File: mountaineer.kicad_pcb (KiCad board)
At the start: 2 copper layers, 50 x 79 mm, 69 parts, among them J1 USB_C_Receptacle, J2 CAT, J3 AUDIO, SW1 VCCIO, U1 TUSB2036, U2 FT232RL, U3 HS-100B, U4 TPS76333, U5 SN75240, U6 TPS2041, Y1 AWSCR-6.00CPLA

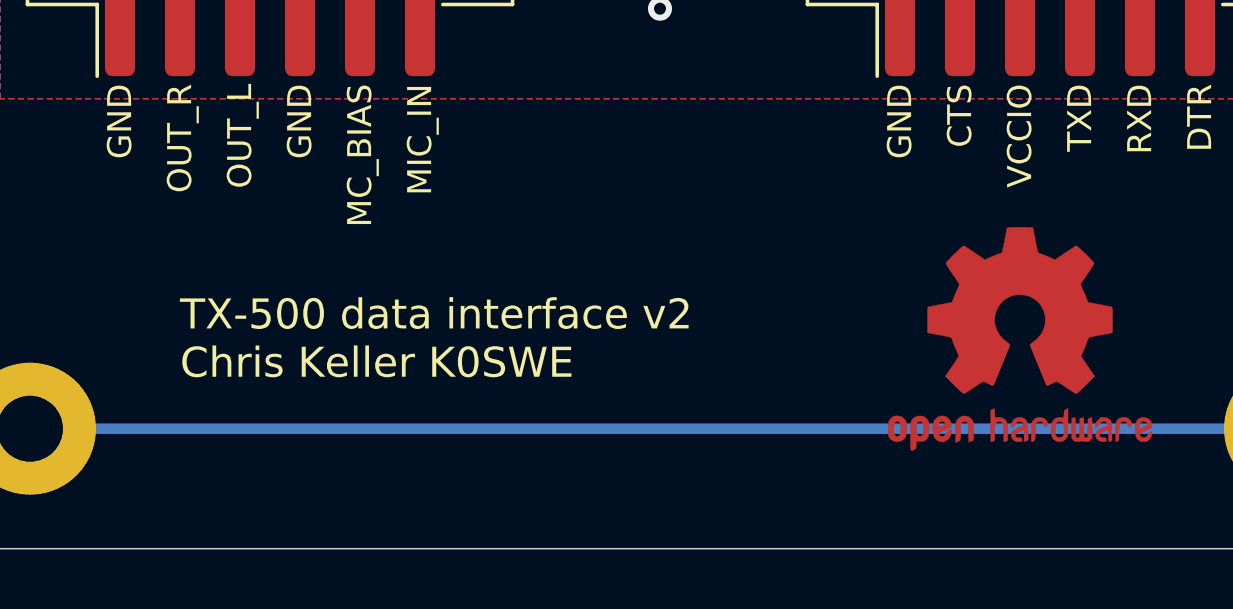
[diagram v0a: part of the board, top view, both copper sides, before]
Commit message: Rename project
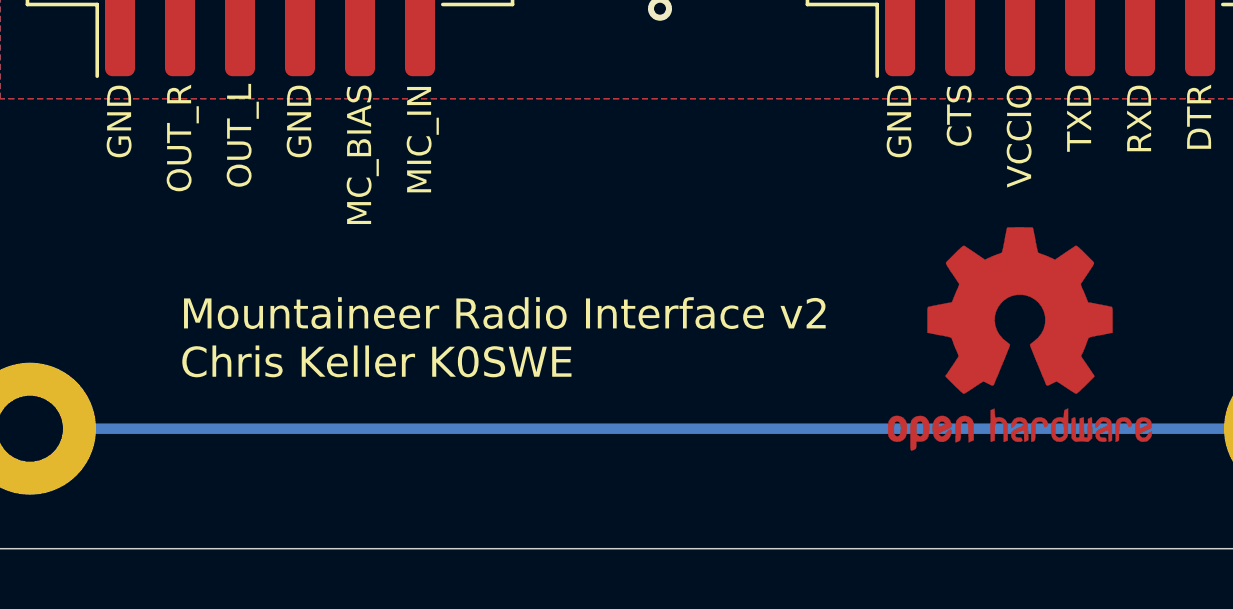
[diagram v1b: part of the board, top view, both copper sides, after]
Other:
- board text added: "Mountaineer Radio Interface v2 Chris Keller K0SWE"
- board text added: "https://github.com/k0swe/mountaineer"
- board text removed: "TX-500 data interface v2 Chris Keller K0SWE"
- board text removed: "https://github.com/k0swe/tx500-data-interface"

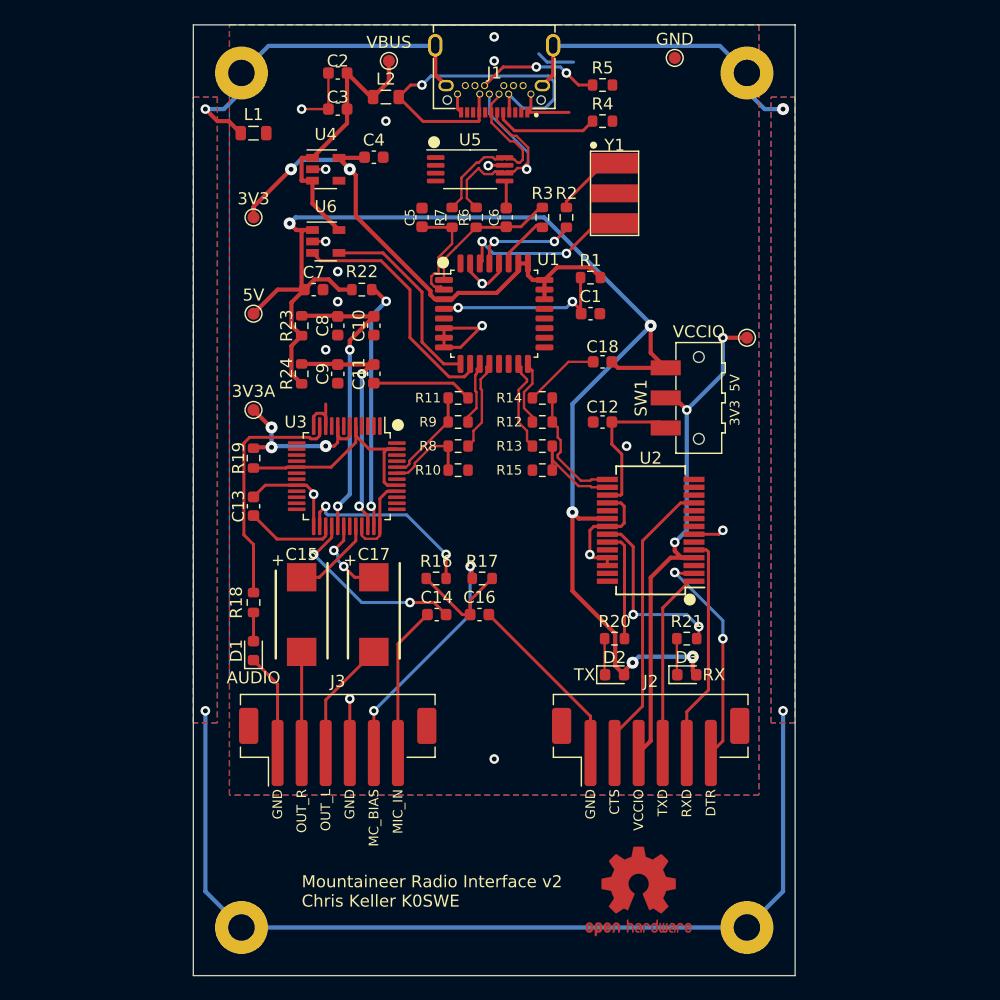
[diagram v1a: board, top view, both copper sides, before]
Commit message: Add pullup resistor to overcurrent protection
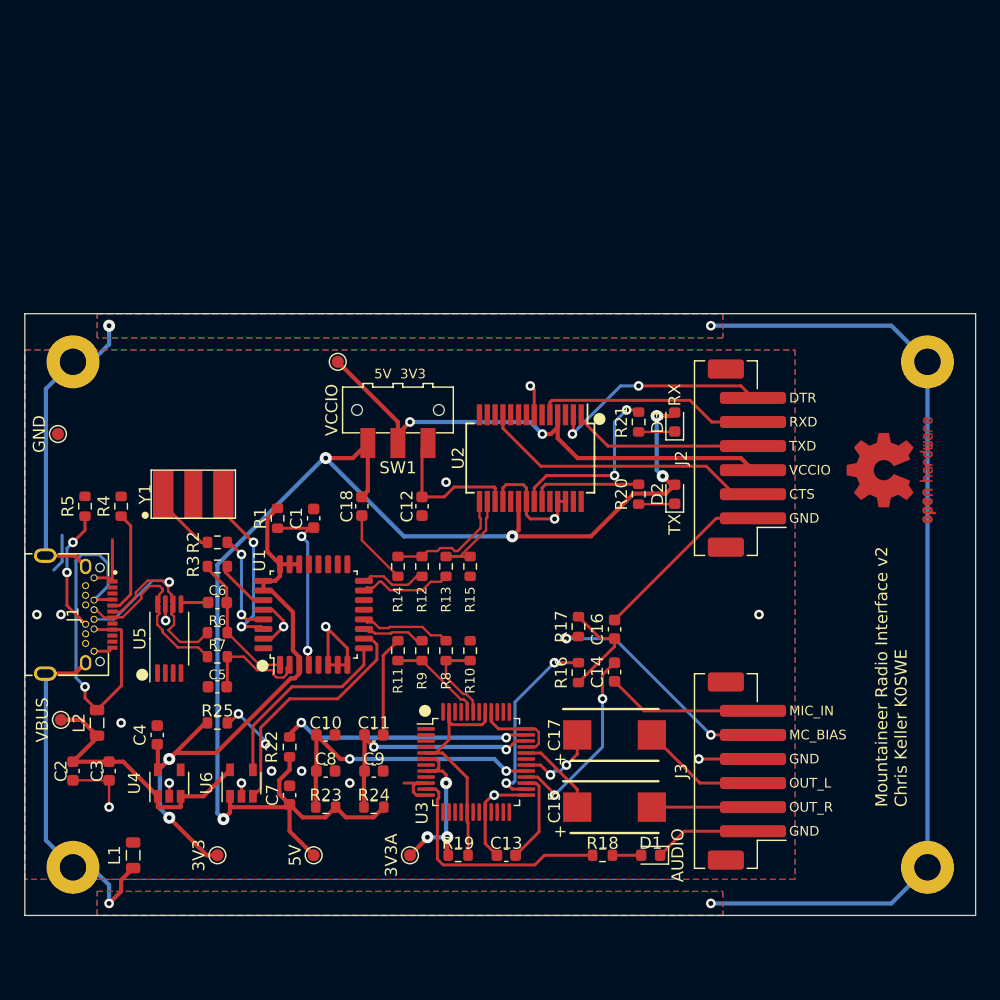
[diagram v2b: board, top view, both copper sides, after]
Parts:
- added R25: 15k, Resistor_SMD:R_0603_1608Metric, F.Cu at (131.0, 116.0)
- moved H1 67.5 mm to (119.0, 128.0), turned to 90 degrees
- moved J1 62.6 mm to (115.0, 107.0), turned to 90 degrees
- moved C2 62.0 mm to (119.0, 120.0), turned to 270 degrees
- moved TP1 61.2 mm to (118.0, 115.8), turned to 270 degrees
- moved H2 60.9 mm to (119.0, 86.0), turned to 90 degrees
- moved L1 60.8 mm to (124.0, 127.0), turned to 90 degrees
- moved TP2 60.0 mm to (117.8, 92.0), turned to 270 degrees
- moved C3 58.2 mm to (122.0, 120.0), turned to 270 degrees
- moved L2 57.3 mm to (121.0, 116.0), turned to 270 degrees
- moved H3 57.2 mm to (190.0, 128.0), turned to 90 degrees
- moved R5 55.4 mm to (120.0, 98.0), turned to 90 degrees
- moved TP3 53.1 mm to (131.0, 127.0), turned to 270 degrees
- moved U4 52.6 mm to (127.0, 121.0), turned to 90 degrees
- moved C4 51.3 mm to (126.0, 117.0), turned to 90 degrees
- moved R4 51.2 mm to (123.0, 98.0), turned to 90 degrees
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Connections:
- net Net-(C1-Pad1) renamed /RESET#
- net Net-(C13-Pad2) renamed /VREF
- net Net-(C14-Pad2) renamed /MICIN
- net Net-(C15-Pad1) renamed /LOR
- net Net-(C17-Pad1) renamed /LOL
- net Net-(R16-Pad2) renamed /VBIAS
- net Net-(R18-Pad2) renamed /LEDO
- net Net-(R19-Pad2) renamed /HIDPU
- net Net-(R2-Pad2) renamed /XTAL2
- net Net-(R3-Pad1) renamed /DP0PUR
- net Net-(U1-Pad10) renamed /OC#
- net Net-(U1-Pad30) renamed /XTAL1
- net Net-(U1-Pad9) renamed /EN#
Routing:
- net /OC#: track 20.5 -> 25.6 mm, vias 0 -> 2
- net +3V3: track 46.9 -> 51.3 mm
- net /VCCIO: track 44.6 -> 44.2 mm, vias 3 -> 2
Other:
- board size 50 x 79 mm -> 79 x 50 mm

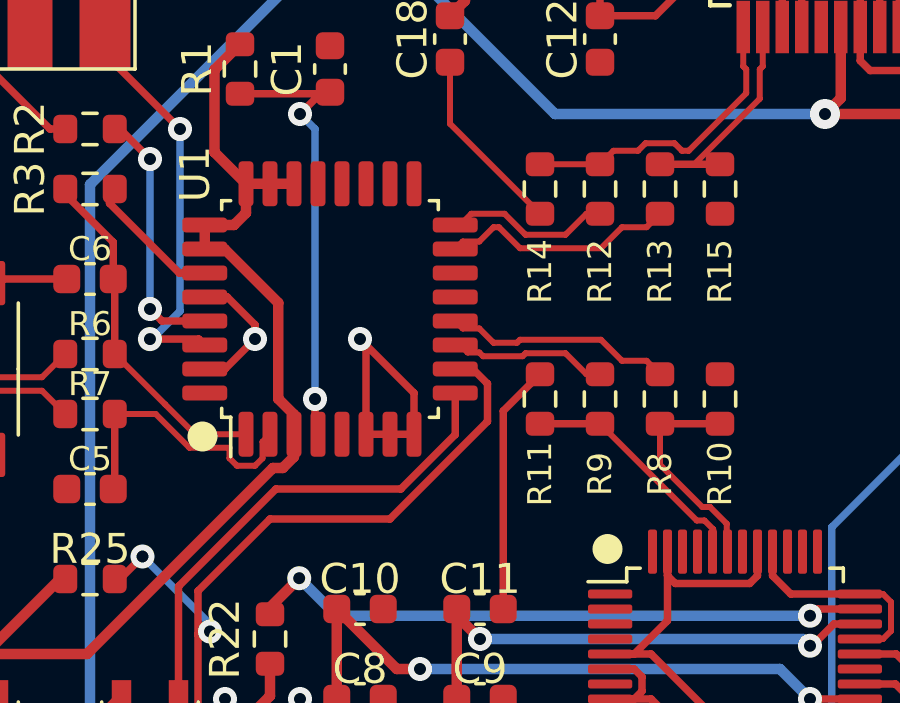
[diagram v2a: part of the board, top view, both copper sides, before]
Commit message: Join all Enable and Overcurrent signals
I think this is the problem that has been bothering me for several weeks. When I replaced the TPS2044B with the TPS2041B, I thought I could use any Enable and any Overcurrent signal, but in that configuration the hub would refuse to power on the downstream ports. After testing this with a breadboard, I think this is the solution.
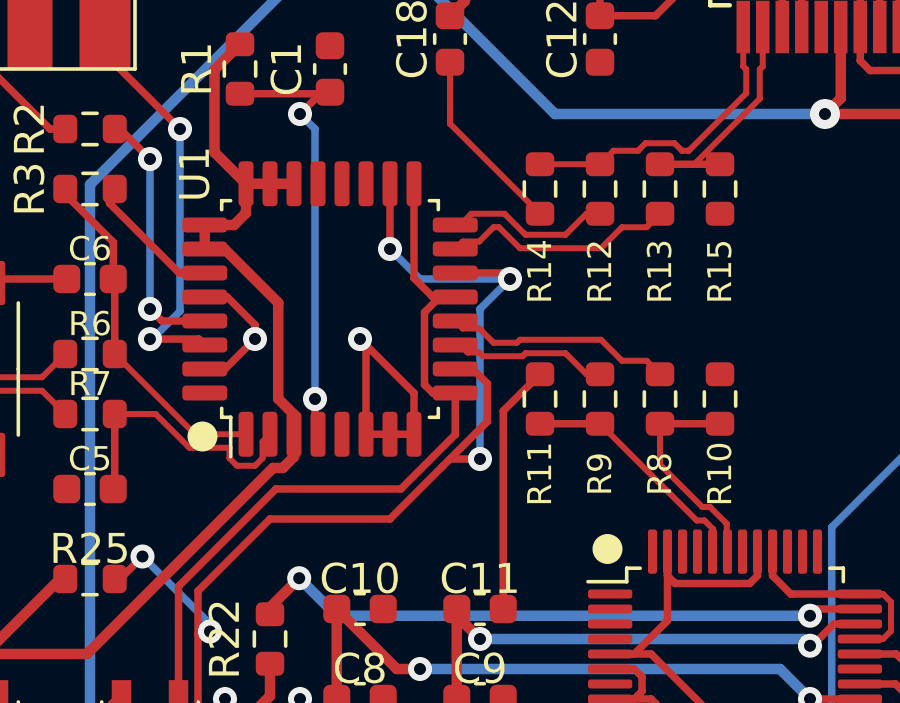
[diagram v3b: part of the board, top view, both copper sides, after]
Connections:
- J1 pad A8: (no net) -> Net-(J1-PadA8)
- J1 pad B8: (no net) -> Net-(J1-PadB8)
- U1 pad 13: (no net) -> /EN#
- U1 pad 14: (no net) -> /OC#
- U1 pad 17: (no net) -> /EN#
- U1 pad 18: (no net) -> /OC#
- U1 pad 19: (no net) -> Net-(U1-Pad19)
- U1 pad 20: (no net) -> Net-(U1-Pad20)
- U1 pad 32: (no net) -> Net-(U1-Pad32)
- U1 pad 5: (no net) -> Net-(U1-Pad5)
- U2 pad 10: (no net) -> Net-(U2-Pad10)
- U2 pad 12: (no net) -> Net-(U2-Pad12)
- U2 pad 13: (no net) -> Net-(U2-Pad13)
- U2 pad 14: (no net) -> Net-(U2-Pad14)
- U2 pad 19: (no net) -> Net-(U2-Pad19)
- U2 pad 27: (no net) -> Net-(U2-Pad27)
- U2 pad 28: (no net) -> Net-(U2-Pad28)
- U2 pad 3: (no net) -> Net-(U2-Pad3)
- U2 pad 6: (no net) -> Net-(U2-Pad6)
- U2 pad 9: (no net) -> Net-(U2-Pad9)
- U3 pad 1: (no net) -> Net-(U3-Pad1)
- U3 pad 19: (no net) -> Net-(U3-Pad19)
- U3 pad 2: (no net) -> Net-(U3-Pad2)
- U3 pad 3: (no net) -> Net-(U3-Pad3)
- U3 pad 31: (no net) -> Net-(U3-Pad31)
- U3 pad 39: (no net) -> Net-(U3-Pad39)
- U3 pad 4: (no net) -> Net-(U3-Pad4)
- U3 pad 42: (no net) -> Net-(U3-Pad42)
- U3 pad 7: (no net) -> Net-(U3-Pad7)
- U4 pad 4: (no net) -> Net-(U4-Pad4)
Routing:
- net /OC#: track 25.6 -> 41.5 mm, vias 2 -> 5
- net /EN#: track 16.4 -> 25.9 mm

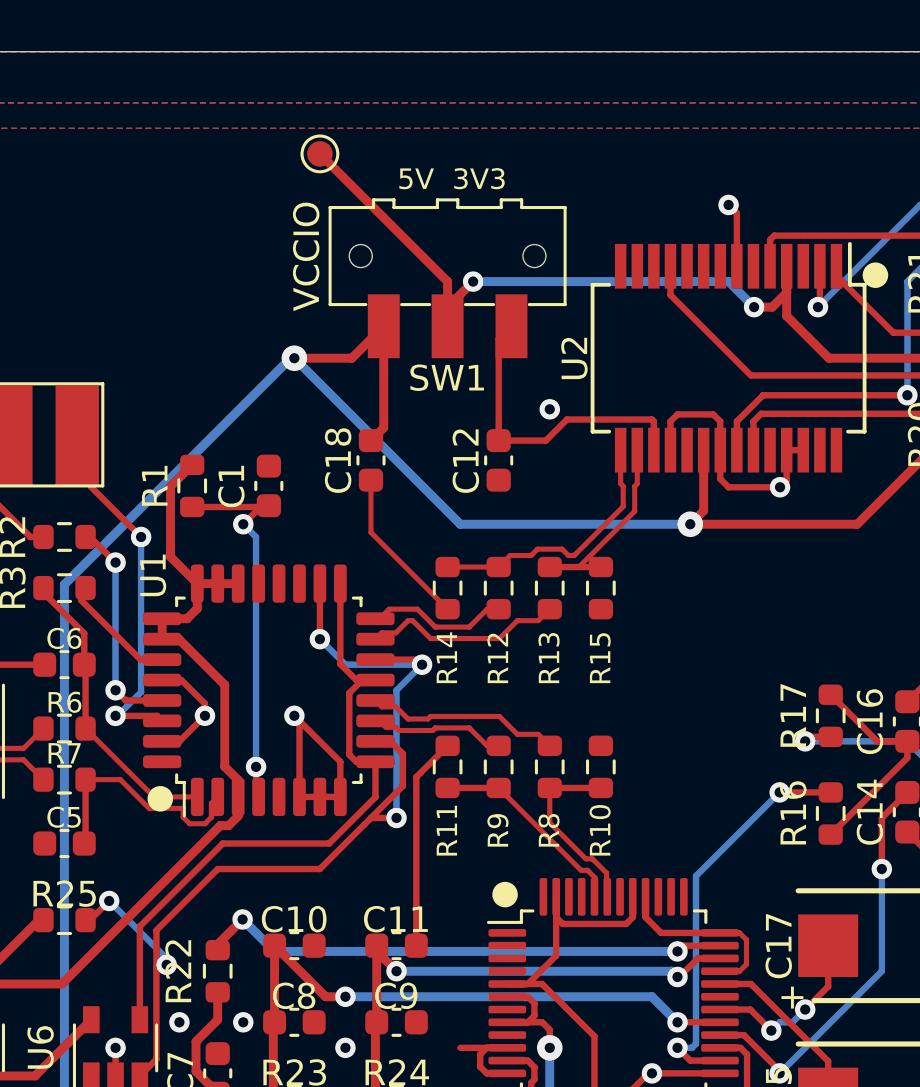
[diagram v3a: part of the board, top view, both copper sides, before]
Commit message: Remove VCCIO switch and add more test points
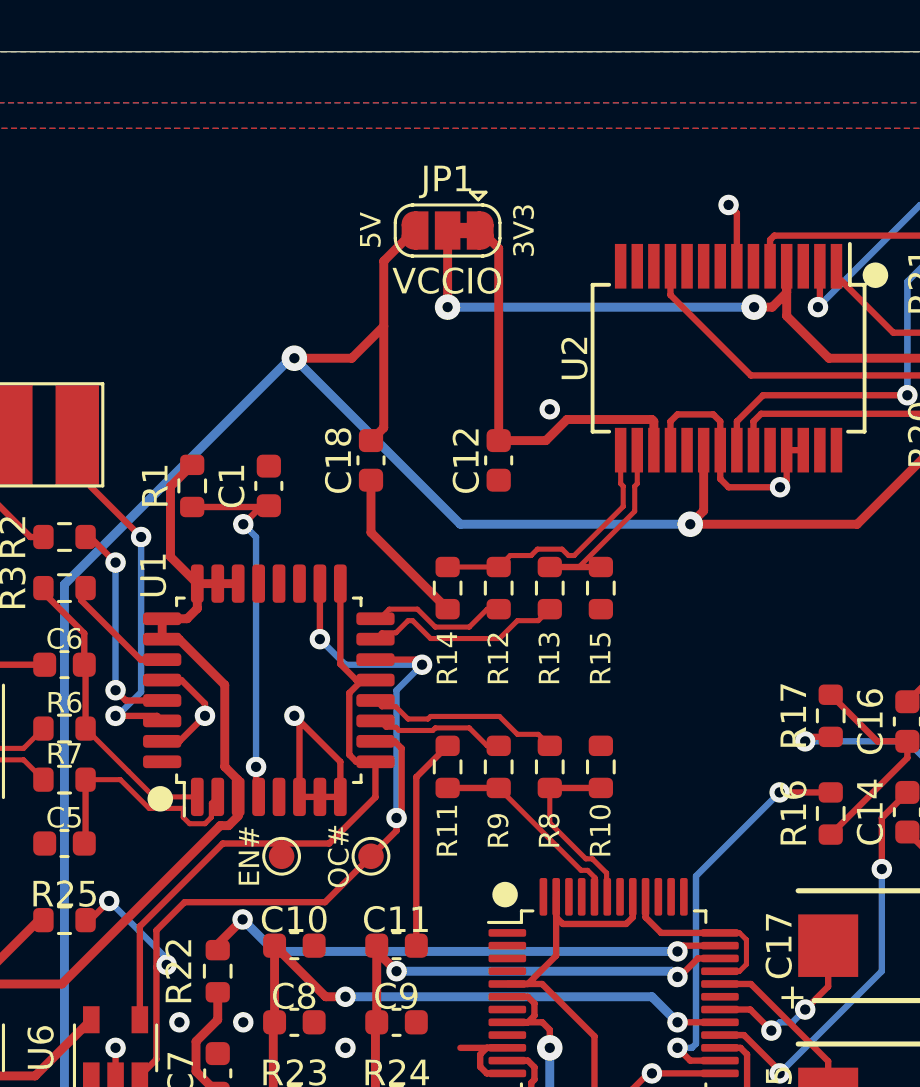
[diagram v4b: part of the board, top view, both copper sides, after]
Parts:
- removed SW1: VCCIO, Button_Switch_SMD:SW_SPDT_CK-JS102011SAQN
- added JP1: VCCIO, Jumper:SolderJumper-3_P1.3mm_Bridged12_RoundedPad1.0x1.5mm, F.Cu at (146.0, 89.0)
- added TP7: EN#, TestPoint:TestPoint_Pad_D1.0mm, F.Cu at (139.5, 113.5)
- R18: value 330R -> 68R
- R20, R21: value 330R -> 150R
- TP5: value VCCIO -> OC#
- moved TP5 27.6 mm to (143.0, 113.5)
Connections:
- J1 pad A8: Net-(J1-PadA8) -> (no net)
- J1 pad B8: Net-(J1-PadB8) -> (no net)
- TP5 pad 1: /VCCIO -> /OC#
- U1 pad 19: Net-(U1-Pad19) -> (no net)
- U1 pad 20: Net-(U1-Pad20) -> (no net)
- U1 pad 32: Net-(U1-Pad32) -> (no net)
- U1 pad 5: Net-(U1-Pad5) -> (no net)
- U2 pad 10: Net-(U2-Pad10) -> (no net)
- U2 pad 12: Net-(U2-Pad12) -> (no net)
- U2 pad 13: Net-(U2-Pad13) -> (no net)
- U2 pad 14: Net-(U2-Pad14) -> (no net)
- U2 pad 19: Net-(U2-Pad19) -> (no net)
- U2 pad 27: Net-(U2-Pad27) -> (no net)
- U2 pad 28: Net-(U2-Pad28) -> (no net)
- U2 pad 3: Net-(U2-Pad3) -> (no net)
- U2 pad 6: Net-(U2-Pad6) -> (no net)
- U2 pad 9: Net-(U2-Pad9) -> (no net)
- U3 pad 1: Net-(U3-Pad1) -> (no net)
- U3 pad 19: Net-(U3-Pad19) -> (no net)
- U3 pad 2: Net-(U3-Pad2) -> (no net)
- U3 pad 3: Net-(U3-Pad3) -> (no net)
- U3 pad 31: Net-(U3-Pad31) -> (no net)
- U3 pad 39: Net-(U3-Pad39) -> (no net)
- U3 pad 4: Net-(U3-Pad4) -> (no net)
- U3 pad 42: Net-(U3-Pad42) -> (no net)
- U3 pad 7: Net-(U3-Pad7) -> (no net)
- U4 pad 4: Net-(U4-Pad4) -> (no net)
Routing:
- net /VCCIO: track 44.2 -> 36.8 mm
- net +5V: track 114.5 -> 118.8 mm
- net /3V3U: track 12.3 -> 16.1 mm
- net /EN#: track 25.9 -> 26.4 mm

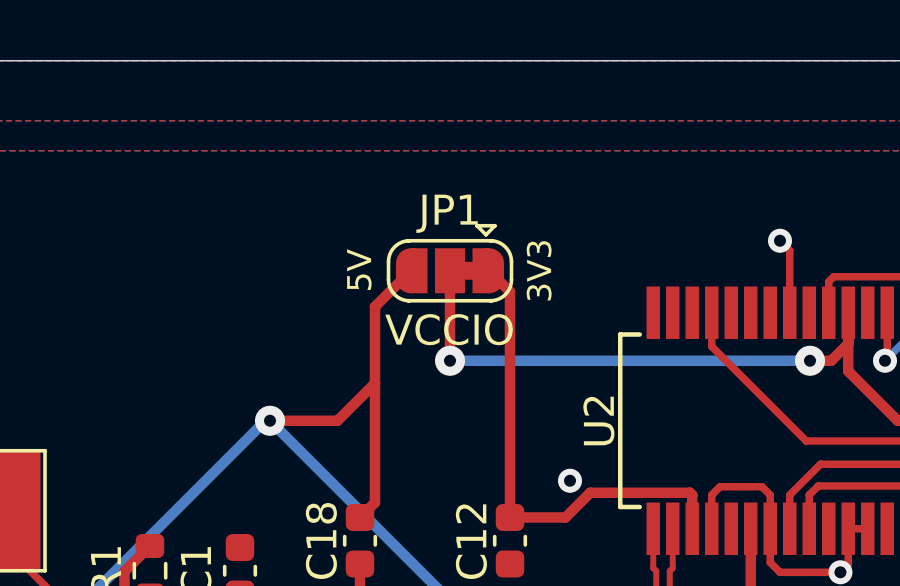
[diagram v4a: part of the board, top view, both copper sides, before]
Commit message: Convert to Kicad 7 project
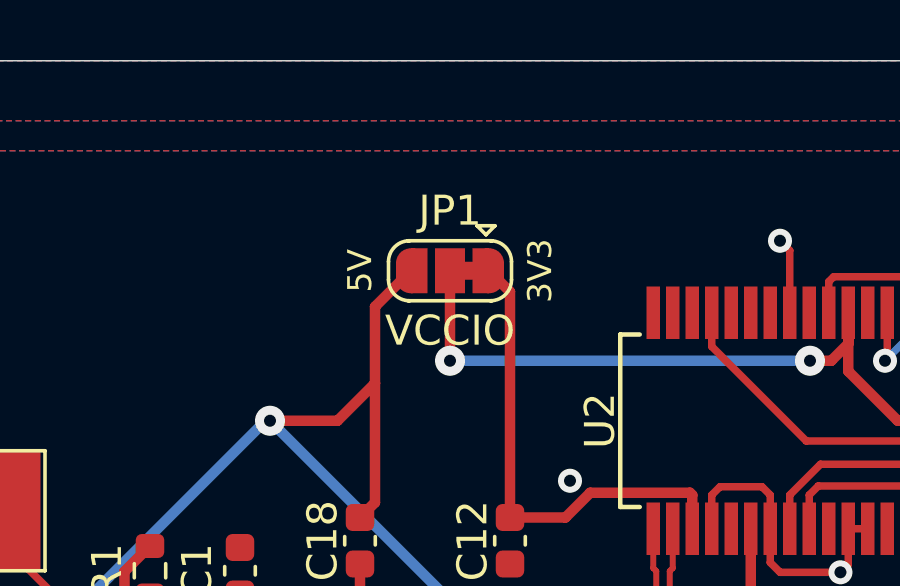
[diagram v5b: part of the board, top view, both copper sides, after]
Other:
- net class Default removed
- net class Power removed
